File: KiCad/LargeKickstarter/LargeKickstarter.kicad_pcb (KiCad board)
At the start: 2 copper layers, 398.2 x 398.2 mm, 294 parts, among them M2 MountingHole_2-5mm, M3 MountingHole_2-5mm, P1 CONN_01X03, P2 CONN_01X02, P3 CONN_01X16, P4 CONN_02X03, SW1 HOUR, SW2 MIN, SW4 SOFT, SW6 RST, U1 HT16K33, U2 DS3231, U3 ATMEGA328-TQFP, U4 HT16K33

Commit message: Full Redesign
Doubled LED count. Added footprints for modules. Still need DS3231
module added.
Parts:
- removed G***: LOGO, LikeClockwork:LOGO_FINAL
- removed P3: CONN_01X16, Pin_Headers:Pin_Header_Straight_1x16
- removed SW6: RST, SparkFun-Electromechanical:TACTILE-PTH-SIDEEZ
- added 0-16: LED, LikeClockwork:SMD_LED_PLCC_2, B.Cu at (398.2, 39.6)
- added 0-17: LED, LikeClockwork:SMD_LED_PLCC_2, B.Cu at (398.2, 63.6)
- added 0-18: LED, LikeClockwork:SMD_LED_PLCC_2, B.Cu at (398.2, 87.6)
- added 0-19: LED, LikeClockwork:SMD_LED_PLCC_2, B.Cu at (398.2, 111.5)
- added 0-20: LED, LikeClockwork:SMD_LED_PLCC_2, B.Cu at (398.2, 135.5)
- added 0-21: LED, LikeClockwork:SMD_LED_PLCC_2, B.Cu at (398.2, 159.5)
- added 0-22: LED, LikeClockwork:SMD_LED_PLCC_2, B.Cu at (398.2, 183.5)
- added 0-23: LED, LikeClockwork:SMD_LED_PLCC_2, B.Cu at (398.2, 207.5)
- added 0-24: LED, LikeClockwork:SMD_LED_PLCC_2, B.Cu at (398.2, 231.5)
- added 0-25: LED, LikeClockwork:SMD_LED_PLCC_2, B.Cu at (398.2, 255.5)
- added 0-26: LED, LikeClockwork:SMD_LED_PLCC_2, B.Cu at (398.2, 279.5)
- added 0-27: LED, LikeClockwork:SMD_LED_PLCC_2, B.Cu at (398.2, 303.5)
- added 0-28: LED, LikeClockwork:SMD_LED_PLCC_2, B.Cu at (398.2, 327.4)
- added 0-29: LED, LikeClockwork:SMD_LED_PLCC_2, B.Cu at (398.2, 351.4)
- added 0-30: LED, LikeClockwork:SMD_LED_PLCC_2, B.Cu at (398.2, 375.4)
- added 0-31: LED, LikeClockwork:SMD_LED_PLCC_2, B.Cu at (398.2, 399.4)
- added 1-16: LED, LikeClockwork:SMD_LED_PLCC_2, B.Cu at (374.2, 39.6)
- added 1-17: LED, LikeClockwork:SMD_LED_PLCC_2, B.Cu at (374.2, 63.6)
- added 1-18: LED, LikeClockwork:SMD_LED_PLCC_2, B.Cu at (374.2, 87.6)
- added 1-19: LED, LikeClockwork:SMD_LED_PLCC_2, B.Cu at (374.2, 111.5)
- added 1-20: LED, LikeClockwork:SMD_LED_PLCC_2, B.Cu at (374.2, 135.5)
- added 1-21: LED, LikeClockwork:SMD_LED_PLCC_2, B.Cu at (374.2, 159.5)
- added 1-22: LED, LikeClockwork:SMD_LED_PLCC_2, B.Cu at (374.2, 183.5)
- added 1-23: LED, LikeClockwork:SMD_LED_PLCC_2, B.Cu at (374.2, 207.5)
- added 1-24: LED, LikeClockwork:SMD_LED_PLCC_2, B.Cu at (374.2, 231.5)
- added 1-25: LED, LikeClockwork:SMD_LED_PLCC_2, B.Cu at (374.2, 255.5)
- added 1-26: LED, LikeClockwork:SMD_LED_PLCC_2, B.Cu at (374.2, 279.5)
- added 1-27: LED, LikeClockwork:SMD_LED_PLCC_2, B.Cu at (374.2, 303.5)
- added 1-28: LED, LikeClockwork:SMD_LED_PLCC_2, B.Cu at (374.2, 327.4)
- added 1-29: LED, LikeClockwork:SMD_LED_PLCC_2, B.Cu at (374.2, 351.4)
- added 1-30: LED, LikeClockwork:SMD_LED_PLCC_2, B.Cu at (374.2, 375.4)
- added 1-31: LED, LikeClockwork:SMD_LED_PLCC_2, B.Cu at (374.2, 399.4)
- added 10-16: LED, LikeClockwork:SMD_LED_PLCC_2, B.Cu at (158.3, 39.6)
- added 10-17: LED, LikeClockwork:SMD_LED_PLCC_2, B.Cu at (158.3, 63.6)
- added 10-18: LED, LikeClockwork:SMD_LED_PLCC_2, B.Cu at (158.3, 87.6)
- added 10-19: LED, LikeClockwork:SMD_LED_PLCC_2, B.Cu at (158.3, 111.5)
- added 10-20: LED, LikeClockwork:SMD_LED_PLCC_2, B.Cu at (158.3, 135.5)
- added 10-21: LED, LikeClockwork:SMD_LED_PLCC_2, B.Cu at (158.3, 159.5)
- added 10-22: LED, LikeClockwork:SMD_LED_PLCC_2, B.Cu at (158.3, 183.5)
- added 10-23: LED, LikeClockwork:SMD_LED_PLCC_2, B.Cu at (158.3, 207.5)
- added 10-24: LED, LikeClockwork:SMD_LED_PLCC_2, B.Cu at (158.3, 231.5)
- added 10-25: LED, LikeClockwork:SMD_LED_PLCC_2, B.Cu at (158.3, 255.5)
- added 10-26: LED, LikeClockwork:SMD_LED_PLCC_2, B.Cu at (158.3, 279.5)
- added 10-27: LED, LikeClockwork:SMD_LED_PLCC_2, B.Cu at (158.3, 303.5)
- added 10-28: LED, LikeClockwork:SMD_LED_PLCC_2, B.Cu at (158.3, 327.4)
- added 10-29: LED, LikeClockwork:SMD_LED_PLCC_2, B.Cu at (158.3, 351.4)
- added 10-30: LED, LikeClockwork:SMD_LED_PLCC_2, B.Cu at (158.3, 375.4)
- added 10-31: LED, LikeClockwork:SMD_LED_PLCC_2, B.Cu at (158.3, 399.4)
- added 11-16: LED, LikeClockwork:SMD_LED_PLCC_2, B.Cu at (134.3, 39.6)
- added 11-17: LED, LikeClockwork:SMD_LED_PLCC_2, B.Cu at (134.3, 63.6)
- added 11-18: LED, LikeClockwork:SMD_LED_PLCC_2, B.Cu at (134.3, 87.6)
- added 11-19: LED, LikeClockwork:SMD_LED_PLCC_2, B.Cu at (134.3, 111.5)
- added 11-20: LED, LikeClockwork:SMD_LED_PLCC_2, B.Cu at (134.3, 135.5)
- added 11-21: LED, LikeClockwork:SMD_LED_PLCC_2, B.Cu at (134.3, 159.5)
- added 11-22: LED, LikeClockwork:SMD_LED_PLCC_2, B.Cu at (134.3, 183.5)
- added 11-23: LED, LikeClockwork:SMD_LED_PLCC_2, B.Cu at (134.3, 207.5)
- added 11-24: LED, LikeClockwork:SMD_LED_PLCC_2, B.Cu at (134.3, 231.5)
- added 11-25: LED, LikeClockwork:SMD_LED_PLCC_2, B.Cu at (134.3, 255.5)
- added 11-26: LED, LikeClockwork:SMD_LED_PLCC_2, B.Cu at (134.3, 279.5)
- added 11-27: LED, LikeClockwork:SMD_LED_PLCC_2, B.Cu at (134.3, 303.5)
- added 11-28: LED, LikeClockwork:SMD_LED_PLCC_2, B.Cu at (134.3, 327.4)
- added 11-29: LED, LikeClockwork:SMD_LED_PLCC_2, B.Cu at (134.3, 351.4)
- added 11-30: LED, LikeClockwork:SMD_LED_PLCC_2, B.Cu at (134.3, 375.4)
- added 11-31: LED, LikeClockwork:SMD_LED_PLCC_2, B.Cu at (134.3, 399.4)
- added 12-16: LED, LikeClockwork:SMD_LED_PLCC_2, B.Cu at (110.3, 39.6)
- added 12-17: LED, LikeClockwork:SMD_LED_PLCC_2, B.Cu at (110.3, 63.6)
- added 12-18: LED, LikeClockwork:SMD_LED_PLCC_2, B.Cu at (110.3, 87.6)
- added 12-19: LED, LikeClockwork:SMD_LED_PLCC_2, B.Cu at (110.3, 111.5)
- added 12-20: LED, LikeClockwork:SMD_LED_PLCC_2, B.Cu at (110.3, 135.5)
- added 12-21: LED, LikeClockwork:SMD_LED_PLCC_2, B.Cu at (110.3, 159.5)
- added 12-22: LED, LikeClockwork:SMD_LED_PLCC_2, B.Cu at (110.3, 183.5)
- added 12-23: LED, LikeClockwork:SMD_LED_PLCC_2, B.Cu at (110.3, 207.5)
- added 12-24: LED, LikeClockwork:SMD_LED_PLCC_2, B.Cu at (110.3, 231.5)
- added 12-25: LED, LikeClockwork:SMD_LED_PLCC_2, B.Cu at (110.3, 255.5)
- added 12-26: LED, LikeClockwork:SMD_LED_PLCC_2, B.Cu at (110.3, 279.5)
- added 12-27: LED, LikeClockwork:SMD_LED_PLCC_2, B.Cu at (110.3, 303.5)
- added 12-28: LED, LikeClockwork:SMD_LED_PLCC_2, B.Cu at (110.3, 327.4)
- added 12-29: LED, LikeClockwork:SMD_LED_PLCC_2, B.Cu at (110.3, 351.4)
- added 12-30: LED, LikeClockwork:SMD_LED_PLCC_2, B.Cu at (110.3, 375.4)
- added 12-31: LED, LikeClockwork:SMD_LED_PLCC_2, B.Cu at (110.3, 399.4)
- added 13-16: LED, LikeClockwork:SMD_LED_PLCC_2, B.Cu at (86.4, 39.6)
- added 13-17: LED, LikeClockwork:SMD_LED_PLCC_2, B.Cu at (86.4, 63.6)
- added 13-18: LED, LikeClockwork:SMD_LED_PLCC_2, B.Cu at (86.4, 87.6)
- added 13-19: LED, LikeClockwork:SMD_LED_PLCC_2, B.Cu at (86.4, 111.5)
- added 13-20: LED, LikeClockwork:SMD_LED_PLCC_2, B.Cu at (86.4, 135.5)
- added 13-21: LED, LikeClockwork:SMD_LED_PLCC_2, B.Cu at (86.4, 159.5)
- added 13-22: LED, LikeClockwork:SMD_LED_PLCC_2, B.Cu at (86.4, 183.5)
- added 13-23: LED, LikeClockwork:SMD_LED_PLCC_2, B.Cu at (86.4, 207.5)
- added 13-24: LED, LikeClockwork:SMD_LED_PLCC_2, B.Cu at (86.4, 231.5)
- added 13-25: LED, LikeClockwork:SMD_LED_PLCC_2, B.Cu at (86.4, 255.5)
- added 13-26: LED, LikeClockwork:SMD_LED_PLCC_2, B.Cu at (86.4, 279.5)
- added 13-27: LED, LikeClockwork:SMD_LED_PLCC_2, B.Cu at (86.4, 303.5)
- added 13-28: LED, LikeClockwork:SMD_LED_PLCC_2, B.Cu at (86.4, 327.4)
- added 13-29: LED, LikeClockwork:SMD_LED_PLCC_2, B.Cu at (86.4, 351.4)
- added 13-30: LED, LikeClockwork:SMD_LED_PLCC_2, B.Cu at (86.4, 375.4)
- added 13-31: LED, LikeClockwork:SMD_LED_PLCC_2, B.Cu at (86.4, 399.4)
- added 14-16: LED, LikeClockwork:SMD_LED_PLCC_2, B.Cu at (62.4, 39.6)
- added 14-17: LED, LikeClockwork:SMD_LED_PLCC_2, B.Cu at (62.4, 63.6)
- added 14-18: LED, LikeClockwork:SMD_LED_PLCC_2, B.Cu at (62.4, 87.6)
- added 14-19: LED, LikeClockwork:SMD_LED_PLCC_2, B.Cu at (62.4, 111.5)
- added 14-20: LED, LikeClockwork:SMD_LED_PLCC_2, B.Cu at (62.4, 135.5)
- added 14-21: LED, LikeClockwork:SMD_LED_PLCC_2, B.Cu at (62.4, 159.5)
- added 14-22: LED, LikeClockwork:SMD_LED_PLCC_2, B.Cu at (62.4, 183.5)
- added 14-23: LED, LikeClockwork:SMD_LED_PLCC_2, B.Cu at (62.4, 207.5)
- added 14-24: LED, LikeClockwork:SMD_LED_PLCC_2, B.Cu at (62.4, 231.5)
- added 14-25: LED, LikeClockwork:SMD_LED_PLCC_2, B.Cu at (62.4, 255.5)
- added 14-26: LED, LikeClockwork:SMD_LED_PLCC_2, B.Cu at (62.4, 279.5)
- added 14-27: LED, LikeClockwork:SMD_LED_PLCC_2, B.Cu at (62.4, 303.5)
- added 14-28: LED, LikeClockwork:SMD_LED_PLCC_2, B.Cu at (62.4, 327.4)
- added 14-29: LED, LikeClockwork:SMD_LED_PLCC_2, B.Cu at (62.4, 351.4)
- added 14-30: LED, LikeClockwork:SMD_LED_PLCC_2, B.Cu at (62.4, 375.4)
- added 14-31: LED, LikeClockwork:SMD_LED_PLCC_2, B.Cu at (62.4, 399.4)
- added 15-16: LED, LikeClockwork:SMD_LED_PLCC_2, B.Cu at (38.4, 39.6)
- added 15-17: LED, LikeClockwork:SMD_LED_PLCC_2, B.Cu at (38.4, 63.6)
- added 15-18: LED, LikeClockwork:SMD_LED_PLCC_2, B.Cu at (38.4, 87.6)
- added 15-19: LED, LikeClockwork:SMD_LED_PLCC_2, B.Cu at (38.4, 111.5)
- added 15-20: LED, LikeClockwork:SMD_LED_PLCC_2, B.Cu at (38.4, 135.5)
- added 15-21: LED, LikeClockwork:SMD_LED_PLCC_2, B.Cu at (38.4, 159.5)
- added 15-22: LED, LikeClockwork:SMD_LED_PLCC_2, B.Cu at (38.4, 183.5)
- added 15-23: LED, LikeClockwork:SMD_LED_PLCC_2, B.Cu at (38.4, 207.5)
- added 15-24: LED, LikeClockwork:SMD_LED_PLCC_2, B.Cu at (38.4, 231.5)
- added 15-25: LED, LikeClockwork:SMD_LED_PLCC_2, B.Cu at (38.4, 255.5)
- added 15-26: LED, LikeClockwork:SMD_LED_PLCC_2, B.Cu at (38.4, 279.5)
- added 15-27: LED, LikeClockwork:SMD_LED_PLCC_2, B.Cu at (38.4, 303.5)
- added 15-28: LED, LikeClockwork:SMD_LED_PLCC_2, B.Cu at (38.4, 327.4)
- added 15-29: LED, LikeClockwork:SMD_LED_PLCC_2, B.Cu at (38.4, 351.4)
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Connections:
- net /Vin1 renamed RAW
- net /Vin2 renamed Vin
- net Net-(0-0-Pad1) renamed ROW-0-0
- net Net-(0-0-Pad2) renamed COM-0-0
- net Net-(0-1-Pad2) renamed COM-0-1
- net Net-(0-10-Pad1) renamed ROW-1-0
- net Net-(0-10-Pad2) renamed COM-1-2
- net Net-(0-11-Pad2) renamed COM-1-3
- net Net-(0-12-Pad2) renamed COM-1-4
- net Net-(0-13-Pad2) renamed COM-1-5
- net Net-(0-14-Pad2) renamed COM-1-6
- net Net-(0-15-Pad2) renamed COM-1-7
- net Net-(0-2-Pad2) renamed COM-0-2
- net Net-(0-3-Pad2) renamed COM-0-3
- net Net-(0-4-Pad2) renamed COM-0-4
- net Net-(0-5-Pad2) renamed COM-0-5
- net Net-(0-6-Pad2) renamed COM-0-6
- net Net-(0-7-Pad2) renamed COM-0-7
- net Net-(0-8-Pad2) renamed COM-1-0
- net Net-(0-9-Pad2) renamed COM-1-1
- net Net-(1-0-Pad1) renamed ROW-0-1
- net Net-(1-10-Pad1) renamed ROW-1-1
- net Net-(10-0-Pad1) renamed ROW-0-10
- net Net-(10-10-Pad1) renamed ROW-1-10
- net Net-(11-0-Pad1) renamed ROW-0-11
- net Net-(11-10-Pad1) renamed ROW-1-11
- net Net-(12-0-Pad1) renamed ROW-0-12
- net Net-(12-10-Pad1) renamed ROW-1-12
- net Net-(13-0-Pad1) renamed ROW-0-13
- net Net-(13-10-Pad1) renamed ROW-1-13
- net Net-(14-0-Pad1) renamed ROW-0-14
- net Net-(14-10-Pad1) renamed ROW-1-14
- net Net-(15-0-Pad1) renamed ROW-0-15
- net Net-(15-10-Pad1) renamed ROW-1-15
- net Net-(2-0-Pad1) renamed ROW-0-2
- net Net-(3-0-Pad1) renamed ROW-0-3
- net Net-(3-10-Pad1) renamed ROW-1-3
- net Net-(4-0-Pad1) renamed ROW-0-4
- net Net-(4-10-Pad1) renamed ROW-1-4
- net Net-(5-0-Pad1) renamed ROW-0-5
- net Net-(5-10-Pad1) renamed ROW-1-5
- net Net-(6-0-Pad1) renamed ROW-0-6
- net Net-(6-10-Pad1) renamed ROW-1-6
- net Net-(7-0-Pad1) renamed ROW-0-7
- net Net-(7-10-Pad1) renamed ROW-1-7
- net Net-(8-0-Pad1) renamed ROW-0-8
- net Net-(8-10-Pad1) renamed ROW-1-8
- net Net-(9-0-Pad1) renamed ROW-0-9
- net Net-(9-10-Pad1) renamed ROW-1-9
- net Net-(R1-Pad1) renamed 5
- net Net-(R2-Pad1) renamed 6
- net Net-(R5-Pad1) renamed 7
- 2-10 pad 1: Net-(2-10-Pad1) -> ROW-1-2
- 2-11 pad 1: Net-(2-10-Pad1) -> ROW-1-2
- 2-12 pad 1: Net-(2-10-Pad1) -> ROW-1-2
- 2-13 pad 1: Net-(2-10-Pad1) -> ROW-1-2
- 2-14 pad 1: Net-(2-10-Pad1) -> ROW-1-2
- 2-15 pad 1: Net-(2-10-Pad1) -> ROW-1-2
- 2-8 pad 1: Net-(2-10-Pad1) -> ROW-1-2
- 2-9 pad 1: Net-(2-10-Pad1) -> ROW-1-2
- R11 pad 1: Net-(2-10-Pad1) -> Net-(JP4-Pad1)
- R8 pad 1: RST -> Net-(JP3-Pad1)
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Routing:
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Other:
- net class Default: clearance 0.3 -> 0.25
- net class Vcc: clearance 0.3 -> 0.25; trace_width 0.3 -> 0.35
- rule trace_clearance: 0.3 -> 0.25
- board text removed: "+5"
- board text removed: "10"
- board text removed: "2"
- board text removed: "8"
- board text removed: "9"
- board text removed: "A0"
- board text removed: "A1"
- board text removed: "A2"
- board text removed: "A3"
- board text removed: "A6"
- board text removed: "A7"
- board text removed: "RX"
- board text removed: "SCL"
- board text removed: "SDA"
- board text removed: "TX"

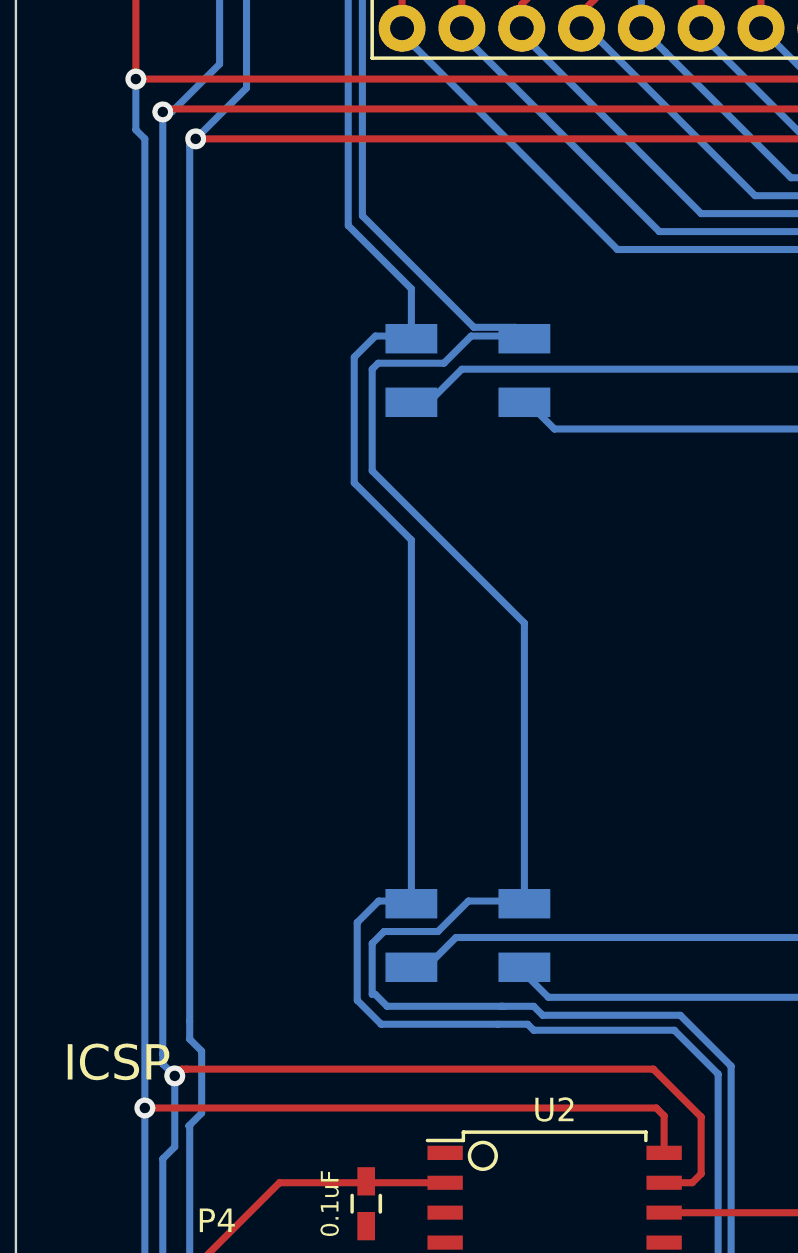
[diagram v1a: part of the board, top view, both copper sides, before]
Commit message: Added DS3231 module footprints
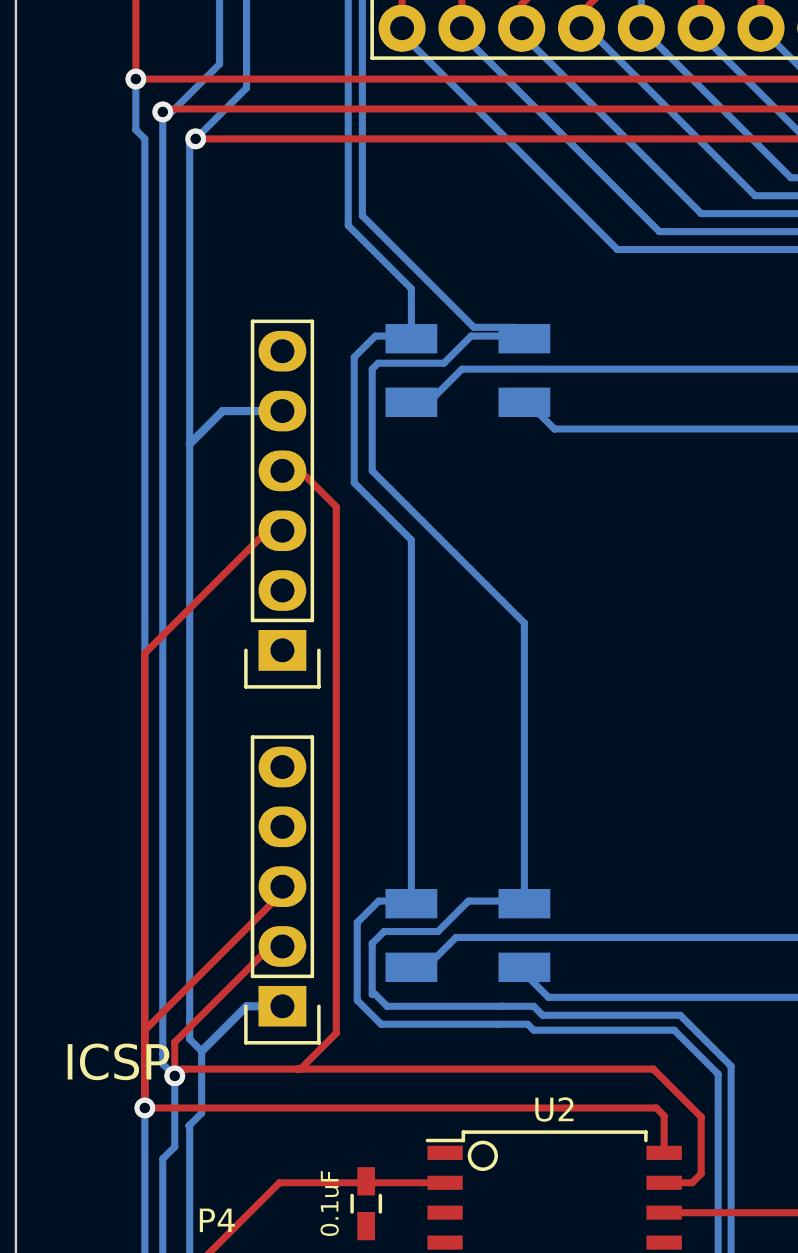
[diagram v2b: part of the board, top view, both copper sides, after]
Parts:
- added P3: CONN_01X05, Pin_Headers:Pin_Header_Straight_1x05, F.Cu at (28.1, 186.5)
- added P5: CONN_01X06, Pin_Headers:Pin_Header_Straight_1x06, F.Cu at (28.1, 171.4)
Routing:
- net SCL: track 661.3 -> 700.4 mm
- net SDA: track 686.8 -> 722.0 mm
- net Vcc: track 815.9 -> 824.6 mm

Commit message: Started on silkscreens
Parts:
- added REF**: solder_pad, LikeClockwork:solder_pad, F.Cu at (260.1, 238.8)
- added REF**: solder_pad, LikeClockwork:solder_pad, F.Cu at (265.2, 238.8)
- added REF**: solder_pad, LikeClockwork:solder_pad, F.Cu at (219.5, 251.5)
- added REF**: solder_pad, LikeClockwork:solder_pad, F.Cu at (255.1, 238.8)
- added REF**: solder_pad, LikeClockwork:solder_pad, F.Cu at (257.6, 236.3)
- added REF**: solder_pad, LikeClockwork:solder_pad, F.Cu at (255.1, 241.4)
- added REF**: solder_pad, LikeClockwork:solder_pad, F.Cu at (257.6, 238.8)
- added REF**: solder_pad, LikeClockwork:solder_pad, F.Cu at (255.1, 236.3)
- added REF**: solder_pad, LikeClockwork:solder_pad, F.Cu at (257.6, 241.4)
- added REF**: solder_pad, LikeClockwork:solder_pad, F.Cu at (255.1, 243.9)
- added REF**: solder_pad, LikeClockwork:solder_pad, F.Cu at (257.6, 243.9)
- added REF**: solder_pad, LikeClockwork:solder_pad, F.Cu at (257.6, 246.5)
- added REF**: solder_pad, LikeClockwork:solder_pad, F.Cu at (267.8, 236.3)
- added REF**: solder_pad, LikeClockwork:solder_pad, F.Cu at (255.1, 246.5)
- added REF**: solder_pad, LikeClockwork:solder_pad, F.Cu at (257.6, 249.0)
- added REF**: solder_pad, LikeClockwork:solder_pad, F.Cu at (257.6, 251.5)
- added REF**: solder_pad, LikeClockwork:solder_pad, F.Cu at (255.1, 249.0)
- added REF**: solder_pad, LikeClockwork:solder_pad, F.Cu at (255.1, 251.5)
- added REF**: solder_pad, LikeClockwork:solder_pad, F.Cu at (238.5, 251.5)
- added REF**: solder_pad, LikeClockwork:solder_pad, F.Cu at (238.5, 249.0)
- added REF**: solder_pad, LikeClockwork:solder_pad, F.Cu at (243.6, 249.0)
- added REF**: solder_pad, LikeClockwork:solder_pad, F.Cu at (241.1, 251.5)
- added REF**: solder_pad, LikeClockwork:solder_pad, F.Cu at (238.5, 238.8)
- added REF**: solder_pad, LikeClockwork:solder_pad, F.Cu at (265.2, 236.3)
- added REF**: solder_pad, LikeClockwork:solder_pad, F.Cu at (238.5, 236.3)
- added REF**: solder_pad, LikeClockwork:solder_pad, F.Cu at (241.1, 236.3)
- added REF**: solder_pad, LikeClockwork:solder_pad, F.Cu at (246.2, 238.8)
- added REF**: solder_pad, LikeClockwork:solder_pad, F.Cu at (243.6, 238.8)
- added REF**: solder_pad, LikeClockwork:solder_pad, F.Cu at (243.6, 236.3)
- added REF**: solder_pad, LikeClockwork:solder_pad, F.Cu at (246.2, 236.3)
- added REF**: solder_pad, LikeClockwork:solder_pad, F.Cu at (243.6, 243.9)
- added REF**: solder_pad, LikeClockwork:solder_pad, F.Cu at (248.7, 246.5)
- added REF**: solder_pad, LikeClockwork:solder_pad, F.Cu at (246.2, 243.9)
- added REF**: solder_pad, LikeClockwork:solder_pad, F.Cu at (246.2, 246.5)
- added REF**: solder_pad, LikeClockwork:solder_pad, F.Cu at (267.8, 238.8)
- added REF**: solder_pad, LikeClockwork:solder_pad, F.Cu at (248.7, 241.4)
- added REF**: solder_pad, LikeClockwork:solder_pad, F.Cu at (246.2, 241.4)
- added REF**: solder_pad, LikeClockwork:solder_pad, F.Cu at (248.7, 238.8)
- added REF**: solder_pad, LikeClockwork:solder_pad, F.Cu at (243.6, 241.4)
- added REF**: solder_pad, LikeClockwork:solder_pad, F.Cu at (248.7, 236.3)
- added REF**: solder_pad, LikeClockwork:solder_pad, F.Cu at (248.7, 243.9)
- added REF**: solder_pad, LikeClockwork:solder_pad, F.Cu at (243.6, 251.5)
- added REF**: solder_pad, LikeClockwork:solder_pad, F.Cu at (246.2, 251.5)
- added REF**: solder_pad, LikeClockwork:solder_pad, F.Cu at (246.2, 249.0)
- added REF**: solder_pad, LikeClockwork:solder_pad, F.Cu at (248.7, 249.0)
- added REF**: solder_pad, LikeClockwork:solder_pad, F.Cu at (270.3, 241.4)
- added REF**: solder_pad, LikeClockwork:solder_pad, F.Cu at (248.7, 251.5)
- added REF**: solder_pad, LikeClockwork:solder_pad, F.Cu at (192.8, 243.9)
- added REF**: solder_pad, LikeClockwork:solder_pad, F.Cu at (192.8, 238.8)
- added REF**: solder_pad, LikeClockwork:solder_pad, F.Cu at (192.8, 241.4)
- added REF**: solder_pad, LikeClockwork:solder_pad, F.Cu at (192.8, 236.3)
- added REF**: solder_pad, LikeClockwork:solder_pad, F.Cu at (200.4, 238.8)
- added REF**: solder_pad, LikeClockwork:solder_pad, F.Cu at (200.4, 241.4)
- added REF**: solder_pad, LikeClockwork:solder_pad, F.Cu at (195.4, 236.3)
- added REF**: solder_pad, LikeClockwork:solder_pad, F.Cu at (200.4, 236.3)
- added REF**: solder_pad, LikeClockwork:solder_pad, F.Cu at (197.9, 236.3)
- added REF**: solder_pad, LikeClockwork:solder_pad, F.Cu at (267.8, 243.9)
- added REF**: solder_pad, LikeClockwork:solder_pad, F.Cu at (197.9, 241.4)
- added REF**: solder_pad, LikeClockwork:solder_pad, F.Cu at (197.9, 238.8)
- added REF**: solder_pad, LikeClockwork:solder_pad, F.Cu at (195.4, 238.8)
- added REF**: solder_pad, LikeClockwork:solder_pad, F.Cu at (195.4, 241.4)
- added REF**: solder_pad, LikeClockwork:solder_pad, F.Cu at (200.4, 251.5)
- added REF**: solder_pad, LikeClockwork:solder_pad, F.Cu at (197.9, 251.5)
- added REF**: solder_pad, LikeClockwork:solder_pad, F.Cu at (197.9, 249.0)
- added REF**: solder_pad, LikeClockwork:solder_pad, F.Cu at (195.4, 249.0)
- added REF**: solder_pad, LikeClockwork:solder_pad, F.Cu at (197.9, 246.5)
- added REF**: solder_pad, LikeClockwork:solder_pad, F.Cu at (195.4, 251.5)
- added REF**: solder_pad, LikeClockwork:solder_pad, F.Cu at (270.3, 243.9)
- added REF**: solder_pad, LikeClockwork:solder_pad, F.Cu at (195.4, 246.5)
- added REF**: solder_pad, LikeClockwork:solder_pad, F.Cu at (200.4, 249.0)
- added REF**: solder_pad, LikeClockwork:solder_pad, F.Cu at (200.4, 243.9)
- added REF**: solder_pad, LikeClockwork:solder_pad, F.Cu at (200.4, 246.5)
- added REF**: solder_pad, LikeClockwork:solder_pad, F.Cu at (197.9, 243.9)
- added REF**: solder_pad, LikeClockwork:solder_pad, F.Cu at (195.4, 243.9)
- added REF**: solder_pad, LikeClockwork:solder_pad, F.Cu at (171.2, 251.5)
- added REF**: solder_pad, LikeClockwork:solder_pad, F.Cu at (171.2, 249.0)
- added REF**: solder_pad, LikeClockwork:solder_pad, F.Cu at (168.7, 251.5)
- added REF**: solder_pad, LikeClockwork:solder_pad, F.Cu at (168.7, 249.0)
- added REF**: solder_pad, LikeClockwork:solder_pad, F.Cu at (267.8, 241.4)
- added REF**: solder_pad, LikeClockwork:solder_pad, F.Cu at (166.2, 251.5)
- added REF**: solder_pad, LikeClockwork:solder_pad, F.Cu at (163.6, 251.5)
- added REF**: solder_pad, LikeClockwork:solder_pad, F.Cu at (163.6, 249.0)
- added REF**: solder_pad, LikeClockwork:solder_pad, F.Cu at (166.2, 249.0)
- added REF**: solder_pad, LikeClockwork:solder_pad, F.Cu at (168.7, 243.9)
- added REF**: solder_pad, LikeClockwork:solder_pad, F.Cu at (171.2, 246.5)
- added REF**: solder_pad, LikeClockwork:solder_pad, F.Cu at (171.2, 243.9)
- added REF**: solder_pad, LikeClockwork:solder_pad, F.Cu at (168.7, 246.5)
- added REF**: solder_pad, LikeClockwork:solder_pad, F.Cu at (161.1, 249.0)
- added REF**: solder_pad, LikeClockwork:solder_pad, F.Cu at (158.5, 251.5)
- added REF**: solder_pad, LikeClockwork:solder_pad, F.Cu at (272.8, 241.4)
- added REF**: solder_pad, LikeClockwork:solder_pad, F.Cu at (158.5, 249.0)
- added REF**: solder_pad, LikeClockwork:solder_pad, F.Cu at (161.1, 251.5)
- added REF**: solder_pad, LikeClockwork:solder_pad, F.Cu at (209.3, 236.3)
- added REF**: solder_pad, LikeClockwork:solder_pad, F.Cu at (206.8, 236.3)
- added REF**: solder_pad, LikeClockwork:solder_pad, F.Cu at (214.4, 241.4)
- added REF**: solder_pad, LikeClockwork:solder_pad, F.Cu at (211.9, 236.3)
- added REF**: solder_pad, LikeClockwork:solder_pad, F.Cu at (214.4, 238.8)
- added REF**: solder_pad, LikeClockwork:solder_pad, F.Cu at (211.9, 238.8)
- added REF**: solder_pad, LikeClockwork:solder_pad, F.Cu at (214.4, 236.3)
- added REF**: solder_pad, LikeClockwork:solder_pad, F.Cu at (211.9, 241.4)
- added REF**: solder_pad, LikeClockwork:solder_pad, F.Cu at (267.8, 249.0)
- added REF**: solder_pad, LikeClockwork:solder_pad, F.Cu at (214.4, 249.0)
- added REF**: solder_pad, LikeClockwork:solder_pad, F.Cu at (214.4, 251.5)
- added REF**: solder_pad, LikeClockwork:solder_pad, F.Cu at (211.9, 249.0)
- added REF**: solder_pad, LikeClockwork:solder_pad, F.Cu at (214.4, 246.5)
- added REF**: solder_pad, LikeClockwork:solder_pad, F.Cu at (211.9, 246.5)
- added REF**: solder_pad, LikeClockwork:solder_pad, F.Cu at (214.4, 243.9)
- added REF**: solder_pad, LikeClockwork:solder_pad, F.Cu at (211.9, 243.9)
- added REF**: solder_pad, LikeClockwork:solder_pad, F.Cu at (211.9, 251.5)
- added REF**: solder_pad, LikeClockwork:solder_pad, F.Cu at (206.8, 243.9)
- added REF**: solder_pad, LikeClockwork:solder_pad, F.Cu at (209.3, 241.4)
- added REF**: solder_pad, LikeClockwork:solder_pad, F.Cu at (260.1, 236.3)
- added REF**: solder_pad, LikeClockwork:solder_pad, F.Cu at (270.3, 251.5)
- added REF**: solder_pad, LikeClockwork:solder_pad, F.Cu at (209.3, 238.8)
- added REF**: solder_pad, LikeClockwork:solder_pad, F.Cu at (206.8, 241.4)
- added REF**: solder_pad, LikeClockwork:solder_pad, F.Cu at (206.8, 238.8)
- added REF**: solder_pad, LikeClockwork:solder_pad, F.Cu at (209.3, 243.9)
- added REF**: solder_pad, LikeClockwork:solder_pad, F.Cu at (206.8, 246.5)
- added REF**: solder_pad, LikeClockwork:solder_pad, F.Cu at (209.3, 246.5)
- added REF**: solder_pad, LikeClockwork:solder_pad, F.Cu at (206.8, 251.5)
- added REF**: solder_pad, LikeClockwork:solder_pad, F.Cu at (209.3, 249.0)
- added REF**: solder_pad, LikeClockwork:solder_pad, F.Cu at (209.3, 251.5)
- added REF**: solder_pad, LikeClockwork:solder_pad, F.Cu at (206.8, 249.0)
- added REF**: solder_pad, LikeClockwork:solder_pad, F.Cu at (272.8, 251.5)
- added REF**: solder_pad, LikeClockwork:solder_pad, F.Cu at (173.8, 251.5)
- added REF**: solder_pad, LikeClockwork:solder_pad, F.Cu at (173.8, 249.0)
- added REF**: solder_pad, LikeClockwork:solder_pad, F.Cu at (176.3, 249.0)
- added REF**: solder_pad, LikeClockwork:solder_pad, F.Cu at (176.3, 251.5)
- added REF**: solder_pad, LikeClockwork:solder_pad, F.Cu at (173.8, 246.5)
- added REF**: solder_pad, LikeClockwork:solder_pad, F.Cu at (176.3, 241.4)
- added REF**: solder_pad, LikeClockwork:solder_pad, F.Cu at (176.3, 246.5)
- added REF**: solder_pad, LikeClockwork:solder_pad, F.Cu at (176.3, 243.9)
- added REF**: solder_pad, LikeClockwork:solder_pad, F.Cu at (173.8, 243.9)
- added REF**: solder_pad, LikeClockwork:solder_pad, F.Cu at (173.8, 241.4)
- added REF**: solder_pad, LikeClockwork:solder_pad, F.Cu at (267.8, 251.5)
- added REF**: solder_pad, LikeClockwork:solder_pad, F.Cu at (171.2, 241.4)
- added REF**: solder_pad, LikeClockwork:solder_pad, F.Cu at (168.7, 238.8)
- added REF**: solder_pad, LikeClockwork:solder_pad, F.Cu at (171.2, 238.8)
- added REF**: solder_pad, LikeClockwork:solder_pad, F.Cu at (168.7, 241.4)
- added REF**: solder_pad, LikeClockwork:solder_pad, F.Cu at (176.3, 238.8)
- added REF**: solder_pad, LikeClockwork:solder_pad, F.Cu at (176.3, 236.3)
- added REF**: solder_pad, LikeClockwork:solder_pad, F.Cu at (173.8, 238.8)
- added REF**: solder_pad, LikeClockwork:solder_pad, F.Cu at (173.8, 236.3)
- added REF**: solder_pad, LikeClockwork:solder_pad, F.Cu at (171.2, 236.3)
- added REF**: solder_pad, LikeClockwork:solder_pad, F.Cu at (168.7, 236.3)
- added REF**: solder_pad, LikeClockwork:solder_pad, F.Cu at (270.3, 249.0)
- added REF**: solder_pad, LikeClockwork:solder_pad, F.Cu at (192.8, 246.5)
- added REF**: solder_pad, LikeClockwork:solder_pad, F.Cu at (192.8, 249.0)
- added REF**: solder_pad, LikeClockwork:solder_pad, F.Cu at (190.3, 251.5)
- added REF**: solder_pad, LikeClockwork:solder_pad, F.Cu at (192.8, 251.5)
- added REF**: solder_pad, LikeClockwork:solder_pad, F.Cu at (190.3, 249.0)
- added REF**: solder_pad, LikeClockwork:solder_pad, F.Cu at (190.3, 246.5)
- added REF**: solder_pad, LikeClockwork:solder_pad, F.Cu at (187.7, 249.0)
- added REF**: solder_pad, LikeClockwork:solder_pad, F.Cu at (187.7, 251.5)
- added REF**: solder_pad, LikeClockwork:solder_pad, F.Cu at (187.7, 246.5)
- added REF**: solder_pad, LikeClockwork:solder_pad, F.Cu at (182.7, 249.0)
- added REF**: solder_pad, LikeClockwork:solder_pad, F.Cu at (272.8, 249.0)
- added REF**: solder_pad, LikeClockwork:solder_pad, F.Cu at (182.7, 251.5)
- added REF**: solder_pad, LikeClockwork:solder_pad, F.Cu at (182.7, 246.5)
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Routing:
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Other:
- board text removed: "GND"
- board text removed: "ICSP"
- board text removed: "Vin"

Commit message: Prelim Gerbers Added
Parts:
- removed the REF** at (260.1, 238.8)
- removed the REF** at (265.2, 238.8)
- removed the REF** at (219.5, 251.5)
- removed the REF** at (255.1, 238.8)
- removed the REF** at (257.6, 236.3)
- removed the REF** at (255.1, 241.4)
- removed the REF** at (257.6, 238.8)
- removed the REF** at (255.1, 236.3)
- removed the REF** at (257.6, 241.4)
- removed the REF** at (255.1, 243.9)
- removed the REF** at (257.6, 243.9)
- removed the REF** at (257.6, 246.5)
- removed the REF** at (267.8, 236.3)
- removed the REF** at (255.1, 246.5)
- removed the REF** at (257.6, 249.0)
- removed the REF** at (257.6, 251.5)
- removed the REF** at (255.1, 249.0)
- removed the REF** at (255.1, 251.5)
- removed the REF** at (238.5, 251.5)
- removed the REF** at (238.5, 249.0)
- removed the REF** at (243.6, 249.0)
- removed the REF** at (241.1, 251.5)
- removed the REF** at (238.5, 238.8)
- removed the REF** at (265.2, 236.3)
- removed the REF** at (238.5, 236.3)
- removed the REF** at (241.1, 236.3)
- removed the REF** at (246.2, 238.8)
- removed the REF** at (243.6, 238.8)
- removed the REF** at (243.6, 236.3)
- removed the REF** at (246.2, 236.3)
- removed the REF** at (243.6, 243.9)
- removed the REF** at (248.7, 246.5)
- removed the REF** at (246.2, 243.9)
- removed the REF** at (246.2, 246.5)
- removed the REF** at (267.8, 238.8)
- removed the REF** at (248.7, 241.4)
- removed the REF** at (246.2, 241.4)
- removed the REF** at (248.7, 238.8)
- removed the REF** at (243.6, 241.4)
- removed the REF** at (248.7, 236.3)
- removed the REF** at (248.7, 243.9)
- removed the REF** at (243.6, 251.5)
- removed the REF** at (246.2, 251.5)
- removed the REF** at (246.2, 249.0)
- removed the REF** at (248.7, 249.0)
- removed the REF** at (270.3, 241.4)
- removed the REF** at (248.7, 251.5)
- removed the REF** at (192.8, 243.9)
- removed the REF** at (192.8, 238.8)
- removed the REF** at (192.8, 241.4)
- removed the REF** at (192.8, 236.3)
- removed the REF** at (200.4, 238.8)
- removed the REF** at (200.4, 241.4)
- removed the REF** at (195.4, 236.3)
- removed the REF** at (200.4, 236.3)
- removed the REF** at (197.9, 236.3)
- removed the REF** at (267.8, 243.9)
- removed the REF** at (197.9, 241.4)
- removed the REF** at (197.9, 238.8)
- removed the REF** at (195.4, 238.8)
- removed the REF** at (195.4, 241.4)
- removed the REF** at (200.4, 251.5)
- removed the REF** at (197.9, 251.5)
- removed the REF** at (197.9, 249.0)
- removed the REF** at (195.4, 249.0)
- removed the REF** at (197.9, 246.5)
- removed the REF** at (195.4, 251.5)
- removed the REF** at (270.3, 243.9)
- removed the REF** at (195.4, 246.5)
- removed the REF** at (200.4, 249.0)
- removed the REF** at (200.4, 243.9)
- removed the REF** at (200.4, 246.5)
- removed the REF** at (197.9, 243.9)
- removed the REF** at (195.4, 243.9)
- removed the REF** at (171.2, 251.5)
- removed the REF** at (171.2, 249.0)
- removed the REF** at (168.7, 251.5)
- removed the REF** at (168.7, 249.0)
- removed the REF** at (267.8, 241.4)
- removed the REF** at (166.2, 251.5)
- removed the REF** at (163.6, 251.5)
- removed the REF** at (163.6, 249.0)
- removed the REF** at (166.2, 249.0)
- removed the REF** at (168.7, 243.9)
- removed the REF** at (171.2, 246.5)
- removed the REF** at (171.2, 243.9)
- removed the REF** at (168.7, 246.5)
- removed the REF** at (161.1, 249.0)
- removed the REF** at (158.5, 251.5)
- removed the REF** at (272.8, 241.4)
- removed the REF** at (158.5, 249.0)
- removed the REF** at (161.1, 251.5)
- removed the REF** at (209.3, 236.3)
- removed the REF** at (206.8, 236.3)
- removed the REF** at (214.4, 241.4)
- removed the REF** at (211.9, 236.3)
- removed the REF** at (214.4, 238.8)
- removed the REF** at (211.9, 238.8)
- removed the REF** at (214.4, 236.3)
- removed the REF** at (211.9, 241.4)
- removed the REF** at (267.8, 249.0)
- removed the REF** at (214.4, 249.0)
- removed the REF** at (214.4, 251.5)
- removed the REF** at (211.9, 249.0)
- removed the REF** at (214.4, 246.5)
- removed the REF** at (211.9, 246.5)
- removed the REF** at (214.4, 243.9)
- removed the REF** at (211.9, 243.9)
- removed the REF** at (211.9, 251.5)
- removed the REF** at (206.8, 243.9)
- removed the REF** at (209.3, 241.4)
- removed the REF** at (260.1, 236.3)
- removed the REF** at (270.3, 251.5)
- removed the REF** at (209.3, 238.8)
- removed the REF** at (206.8, 241.4)
- removed the REF** at (206.8, 238.8)
- removed the REF** at (209.3, 243.9)
- removed the REF** at (206.8, 246.5)
- removed the REF** at (209.3, 246.5)
- removed the REF** at (206.8, 251.5)
- removed the REF** at (209.3, 249.0)
- removed the REF** at (209.3, 251.5)
- removed the REF** at (206.8, 249.0)
- removed the REF** at (272.8, 251.5)
- removed the REF** at (173.8, 251.5)
- removed the REF** at (173.8, 249.0)
- removed the REF** at (176.3, 249.0)
- removed the REF** at (176.3, 251.5)
- removed the REF** at (173.8, 246.5)
- removed the REF** at (176.3, 241.4)
- removed the REF** at (176.3, 246.5)
- removed the REF** at (176.3, 243.9)
- removed the REF** at (173.8, 243.9)
- removed the REF** at (173.8, 241.4)
- removed the REF** at (267.8, 251.5)
- removed the REF** at (171.2, 241.4)
- removed the REF** at (168.7, 238.8)
- removed the REF** at (171.2, 238.8)
- removed the REF** at (168.7, 241.4)
- removed the REF** at (176.3, 238.8)
- removed the REF** at (176.3, 236.3)
- removed the REF** at (173.8, 238.8)
- removed the REF** at (173.8, 236.3)
- removed the REF** at (171.2, 236.3)
- removed the REF** at (168.7, 236.3)
- removed the REF** at (270.3, 249.0)
- removed the REF** at (192.8, 246.5)
- removed the REF** at (192.8, 249.0)
- removed the REF** at (190.3, 251.5)
- removed the REF** at (192.8, 251.5)
- removed the REF** at (190.3, 249.0)
- removed the REF** at (190.3, 246.5)
- removed the REF** at (187.7, 249.0)
- removed the REF** at (187.7, 251.5)
- removed the REF** at (187.7, 246.5)
- removed the REF** at (182.7, 249.0)
- removed the REF** at (272.8, 249.0)
- removed the REF** at (182.7, 251.5)
- removed the REF** at (182.7, 246.5)
- removed the REF** at (185.2, 249.0)
- removed the REF** at (185.2, 251.5)
- removed the REF** at (185.2, 246.5)
- removed the REF** at (187.7, 241.4)
- removed the REF** at (190.3, 241.4)
- removed the REF** at (190.3, 243.9)
- removed the REF** at (187.7, 243.9)
- removed the REF** at (185.2, 238.8)
- removed the REF** at (265.2, 249.0)
- removed the REF** at (185.2, 236.3)
- removed the REF** at (182.7, 236.3)
- removed the REF** at (182.7, 238.8)
- removed the REF** at (182.7, 243.9)
- removed the REF** at (185.2, 241.4)
- removed the REF** at (182.7, 241.4)
- removed the REF** at (185.2, 243.9)
- removed the REF** at (190.3, 238.8)
- removed the REF** at (187.7, 236.3)
- removed the REF** at (190.3, 236.3)
- removed the REF** at (262.7, 251.5)
- removed the REF** at (187.7, 238.8)
- removed the REF** at (163.6, 246.5)
- removed the REF** at (166.2, 246.5)
- removed the REF** at (166.2, 243.9)
- removed the REF** at (163.6, 243.9)
- removed the REF** at (158.5, 236.3)
- removed the REF** at (158.5, 238.8)
- removed the REF** at (161.1, 238.8)
- removed the REF** at (161.1, 236.3)
- removed the REF** at (166.2, 241.4)
- removed the REF** at (265.2, 251.5)
- removed the REF** at (163.6, 236.3)
- removed the REF** at (163.6, 238.8)
- removed the REF** at (166.2, 236.3)
- removed the REF** at (163.6, 241.4)
- removed the REF** at (166.2, 238.8)
- removed the REF** at (158.5, 246.5)
- removed the REF** at (158.5, 241.4)
- removed the REF** at (161.1, 241.4)
- removed the REF** at (158.5, 243.9)
- removed the REF** at (161.1, 243.9)
- removed the REF** at (260.1, 249.0)
- removed the REF** at (161.1, 246.5)
- removed the REF** at (255.1, 195.7)
- removed the REF** at (255.1, 190.6)
- removed the REF** at (255.1, 188.0)
- removed the REF** at (255.1, 193.1)
- removed the REF** at (257.6, 195.7)
- removed the REF** at (257.6, 193.1)
- removed the REF** at (257.6, 188.0)
- removed the REF** at (260.1, 190.6)
- removed the REF** at (265.2, 193.1)
- removed the REF** at (262.7, 249.0)
- removed the REF** at (265.2, 190.6)
- removed the REF** at (260.1, 188.0)
- removed the REF** at (257.6, 190.6)
- removed the REF** at (257.6, 198.2)
- removed the REF** at (255.1, 198.2)
- removed the REF** at (255.1, 203.3)
- removed the REF** at (257.6, 200.7)
- removed the REF** at (257.6, 203.3)
- removed the REF** at (255.1, 200.7)
- removed the REF** at (260.1, 203.3)
- removed the REF** at (262.7, 238.8)
- removed the REF** at (265.2, 246.5)
- removed the REF** at (262.7, 203.3)
- removed the REF** at (260.1, 195.7)
- removed the REF** at (262.7, 195.7)
- removed the REF** at (262.7, 193.1)
- removed the REF** at (265.2, 195.7)
- removed the REF** at (260.1, 193.1)
- removed the REF** at (267.8, 200.7)
- removed the REF** at (270.3, 203.3)
- removed the REF** at (270.3, 200.7)
- removed the REF** at (265.2, 203.3)
- removed the REF** at (260.1, 251.5)
- removed the REF** at (267.8, 203.3)
- removed the REF** at (262.7, 190.6)
- removed the REF** at (267.8, 190.6)
- removed the REF** at (267.8, 188.0)
- removed the REF** at (262.7, 188.0)
- removed the REF** at (265.2, 188.0)
- removed the REF** at (270.3, 190.6)
- removed the REF** at (270.3, 188.0)
- removed the REF** at (270.3, 193.1)
- removed the REF** at (272.8, 193.1)
- removed the REF** at (262.7, 241.4)
- removed the REF** at (272.8, 188.0)
- removed the REF** at (272.8, 190.6)
- removed the REF** at (267.8, 193.1)
- removed the REF** at (267.8, 198.2)
- removed the REF** at (267.8, 195.7)
- removed the REF** at (272.8, 198.2)
- removed the REF** at (270.3, 195.7)
- removed the REF** at (270.3, 198.2)
- removed the REF** at (272.8, 203.3)
- removed the REF** at (272.8, 195.7)
- removed the REF** at (260.1, 241.4)
- removed the REF** at (272.8, 200.7)
- removed the REF** at (260.1, 198.2)
- removed the REF** at (262.7, 200.7)
- removed the REF** at (260.1, 200.7)
- removed the REF** at (262.7, 198.2)
- removed the REF** at (265.2, 198.2)
- removed the REF** at (265.2, 200.7)
- removed the REF** at (233.5, 198.2)
- removed the REF** at (230.9, 200.7)
- removed the REF** at (230.9, 203.3)
- removed the REF** at (260.1, 243.9)
- removed the REF** at (230.9, 198.2)
- removed the REF** at (233.5, 203.3)
- removed the REF** at (233.5, 200.7)
- removed the REF** at (236.0, 198.2)
- removed the REF** at (236.0, 200.7)
- removed the REF** at (236.0, 203.3)
- removed the REF** at (238.5, 200.7)
- removed the REF** at (238.5, 203.3)
- removed the REF** at (238.5, 198.2)
- removed the REF** at (233.5, 195.7)
- removed the REF** at (262.7, 243.9)
- removed the REF** at (230.9, 195.7)
- removed the REF** at (230.9, 190.6)
- removed the REF** at (233.5, 193.1)
- removed the REF** at (230.9, 193.1)
- removed the REF** at (236.0, 195.7)
- removed the REF** at (236.0, 193.1)
- removed the REF** at (238.5, 195.7)
- removed the REF** at (238.5, 193.1)
- removed the REF** at (241.1, 195.7)
- removed the REF** at (230.9, 188.0)
- removed the REF** at (265.2, 243.9)
- removed the REF** at (233.5, 188.0)
- removed the REF** at (236.0, 190.6)
- removed the REF** at (238.5, 190.6)
- removed the REF** at (236.0, 188.0)
- removed the REF** at (238.5, 188.0)
- removed the REF** at (233.5, 190.6)
- removed the REF** at (246.2, 190.6)
- removed the REF** at (248.7, 190.6)
- removed the REF** at (246.2, 193.1)
- removed the REF** at (248.7, 193.1)
- removed the REF** at (260.1, 246.5)
- removed the REF** at (241.1, 198.2)
- removed the REF** at (243.6, 200.7)
- removed the REF** at (241.1, 200.7)
- removed the REF** at (243.6, 203.3)
- removed the REF** at (241.1, 203.3)
- removed the REF** at (243.6, 193.1)
- removed the REF** at (246.2, 188.0)
- removed the REF** at (243.6, 188.0)
- removed the REF** at (241.1, 188.0)
- removed the REF** at (243.6, 190.6)
- removed the REF** at (262.7, 246.5)
- removed the REF** at (241.1, 193.1)
- removed the REF** at (248.7, 188.0)
- removed the REF** at (241.1, 190.6)
- removed the REF** at (243.6, 198.2)
- removed the REF** at (243.6, 195.7)
- removed the REF** at (246.2, 195.7)
- removed the REF** at (246.2, 198.2)
- removed the REF** at (248.7, 198.2)
- removed the REF** at (248.7, 195.7)
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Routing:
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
